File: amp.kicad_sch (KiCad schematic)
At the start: 20 parts, among them CN1 MX128-5.0-04P-GN01-CU-Y-A, Q2 CZT5551, Q4 CZT5401, U4 LTC6090CS8E-5#TRPBF

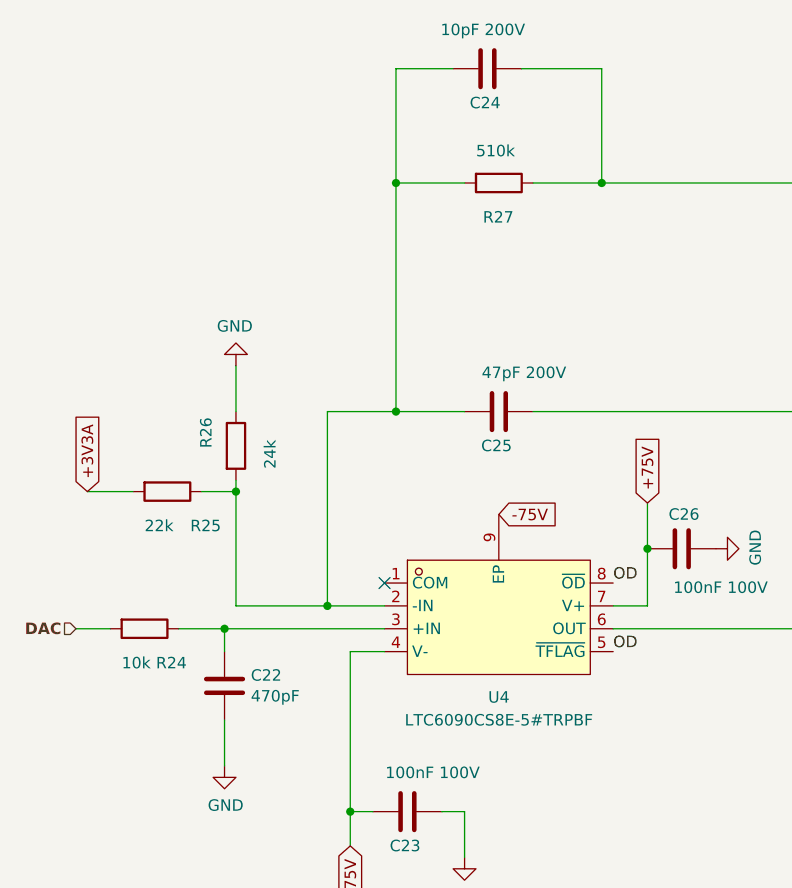
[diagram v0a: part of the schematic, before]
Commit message: fix work for piezo and step driver
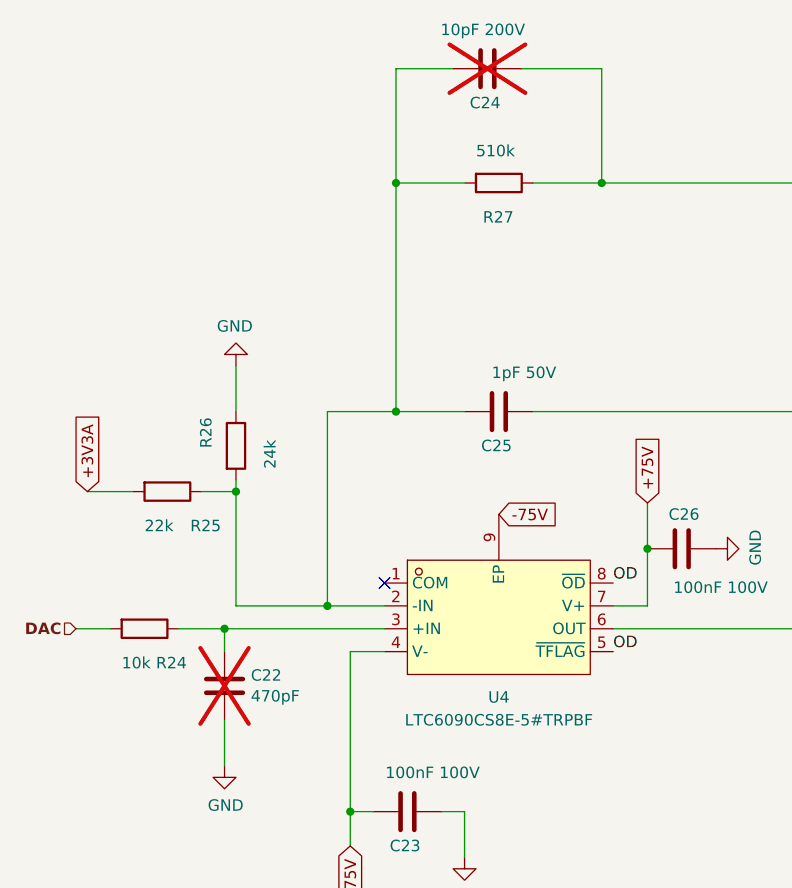
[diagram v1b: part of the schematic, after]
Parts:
- C22, C24: now not fitted
- C25: value 47pF 200V -> 1pF 50V; LCSC C5186754 -> C1786
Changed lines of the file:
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@@
 		(in_bom yes)
 		(on_board yes)
-		(dnp no)
+		(dnp yes)
 		(property "Reference" "C22"
 			(at 46.101 105.5116 0)
@@
 			)
 		)
-		(property "Value" "47pF 200V"
+		(property "Value" "1pF 50V"
 			(at 76.454 71.882 90)
 			(effects
@@
 			)
 		)
-		(property "LCSC" "C5186754"
+		(property "LCSC" "C1786"
 			(at 73.66 76.2 0)
 			(effects
@@
 		(in_bom yes)
 		(on_board yes)
-		(dnp no)
+		(dnp yes)
 		(property "Reference" "C24"
 			(at 72.136 41.91 90)
